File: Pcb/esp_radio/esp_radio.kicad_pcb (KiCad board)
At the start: 2 copper layers, 145.4 x 136.5 mm, 160 parts, among them J1 Power 10V, J10 LCD SPI, J2 JTAG_ESP1, J3 Antenna, J4 USB_B_Micro, J5 GPIOB, J6 GPIOA, J7 MERUS I2S, J8 MERUS I2C, J9 LCD I2C, Q1 SS8050G, Q2 SS8050G, Q3 AO3415A, Q4 SS8050G, SW1 Reset, SW2 Boot, SW3 Prev, SW4 Play, SW5 Next, SW6 RotaryEncoder_Switch, U1 AMS1117-5, U10 AMS1117-1.8, U2 AMS1117-3.3, U3 ESP32-WROVER_IE, U4 VS1053, U5 RDA5807FP, U6 CH340C, U7 MCP23017_SO, U8 74HC157, U9 74HC157, Y1 12.288Mhz, Y2 32.768kHz

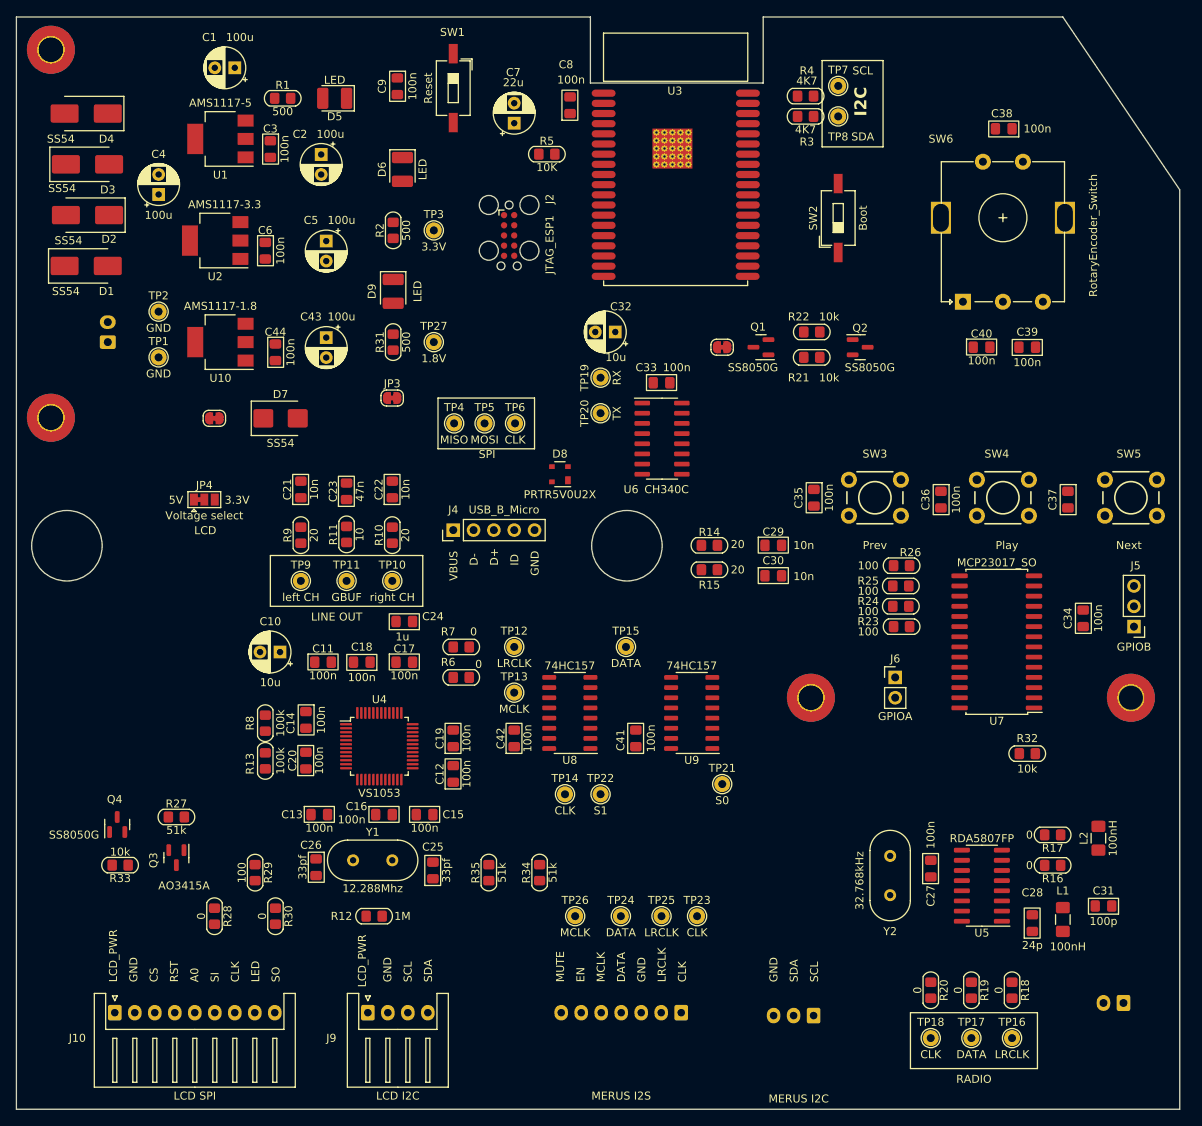
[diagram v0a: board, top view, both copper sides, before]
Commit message: Partially route board
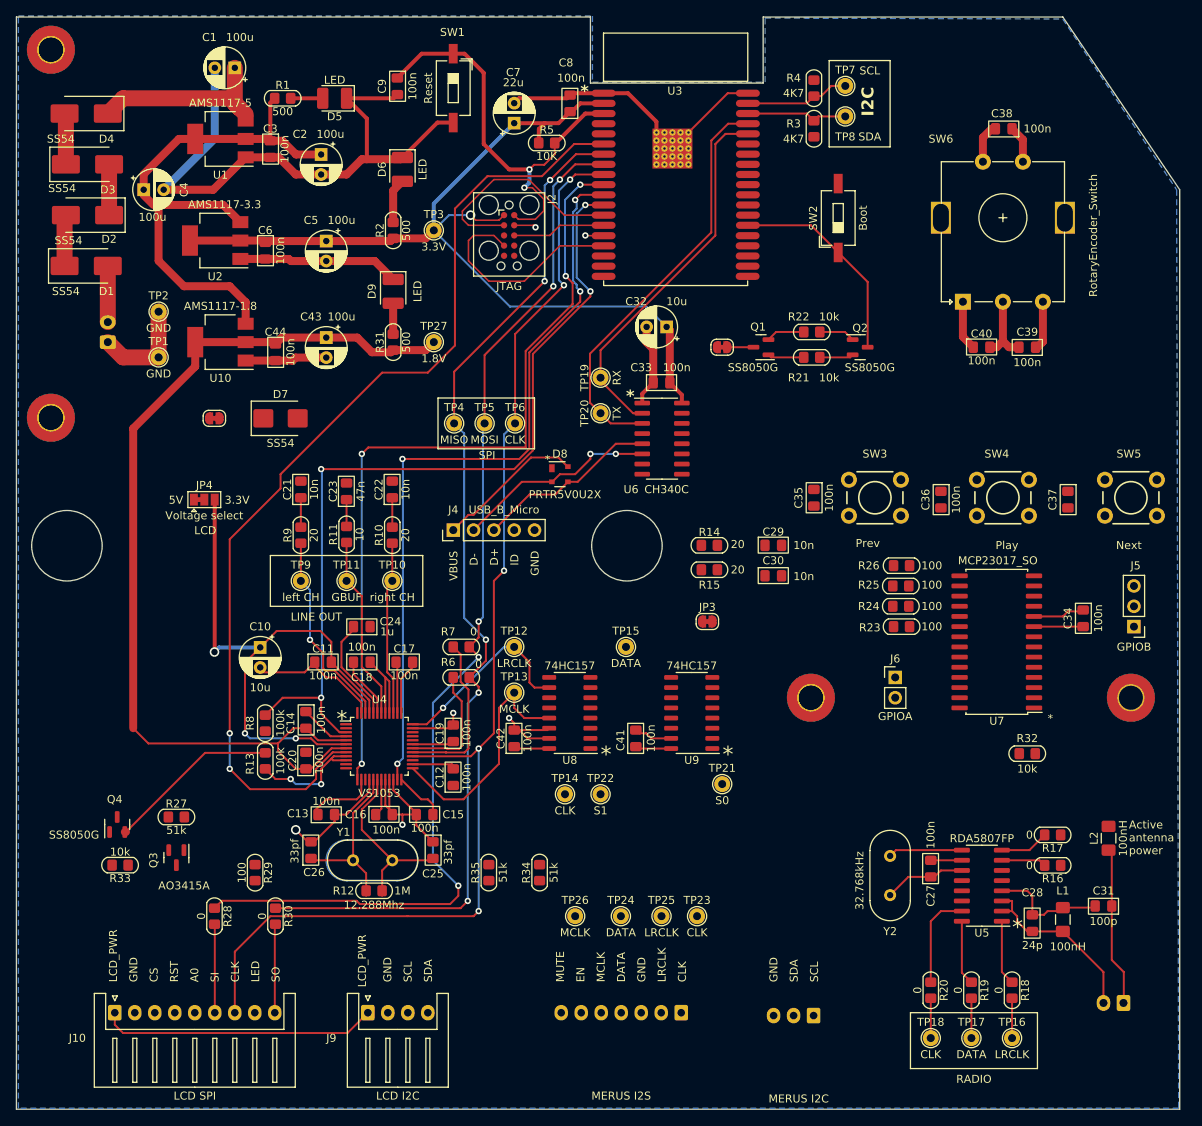
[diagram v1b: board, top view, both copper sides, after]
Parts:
- J2: value JTAG_ESP1 -> JTAG
- moved JP3 48.3 mm to (176.5, 94.6)
- moved C32 6.45 mm to (171.4, 57.8)
- moved C24 5.35 mm to (133.3, 95.2)
- moved R12 3.17 mm to (134.9, 128.3)
- moved C25 2.54 mm to (142.2, 123.2), turned to -90 degrees
- moved C10 2.54 mm to (120.7, 97.9), turned to -90 degrees
- moved C26 2.23 mm to (127.0, 123.2), turned to 90 degrees
- moved C4 1.96 mm to (106.1, 40.6), turned to 0 degrees
- moved R3 1.87 mm to (189.9, 33.0), turned to 90 degrees
- moved R4 1.44 mm to (189.9, 27.9), turned to -90 degrees
- moved R5 1.40 mm to (156.5, 34.8)
- moved L2 1.27 mm to (226.7, 121.7)
- moved TP7 0.88 mm to (193.8, 27.7)
- moved TP8 0.88 mm to (193.8, 31.5)
- moved C13 0.87 mm to (128.9, 118.7), turned to 180 degrees
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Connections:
- ? pad 1: (no net) -> GND (x3)
- REF** pad 1: (no net) -> GND (x4)
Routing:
- net GND: track 0.00 -> 340.4 mm, vias 0 -> 6
- net +3.3V: track 0.00 -> 240.9 mm, vias 0 -> 4
- net /Audio Decoder/SPI.CLK: track 0.00 -> 150.0 mm, vias 0 -> 5
- net /Audio Decoder/SPI.MOSI: track 0.00 -> 136.1 mm, vias 0 -> 5
- net +1V8: track 0.00 -> 134.5 mm
- net /Audio Decoder/SPI.MISO: track 0.00 -> 131.1 mm, vias 0 -> 5
- net /Audio Decoder/VS1053.DREQ: track 0.00 -> 125.2 mm, vias 0 -> 2
- net /Audio Decoder/VS1053.RST: track 0.00 -> 107.2 mm, vias 0 -> 4
- net /Audio Decoder/VS1053.XDCS: track 0.00 -> 101.1 mm, vias 0 -> 4
- net /Audio Decoder/VS1053.XCS: track 0.00 -> 95.0 mm, vias 0 -> 4
- net +5V: track 0.00 -> 69.2 mm
- net /ESP_board/JTAG.RESET: track 0.00 -> 53.3 mm, vias 0 -> 2
- net /ESP_board/UART.TX: track 0.00 -> 52.1 mm
- net /ESP_board/UART.RX: track 0.00 -> 47.0 mm
- net /LCD screen/LCD_PWR: track 0.00 -> 34.6 mm
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- added copper zone on B.Cu, net GND
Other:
- board text added: "*"
- board text added: "Active antenna power"

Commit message: Additional routing
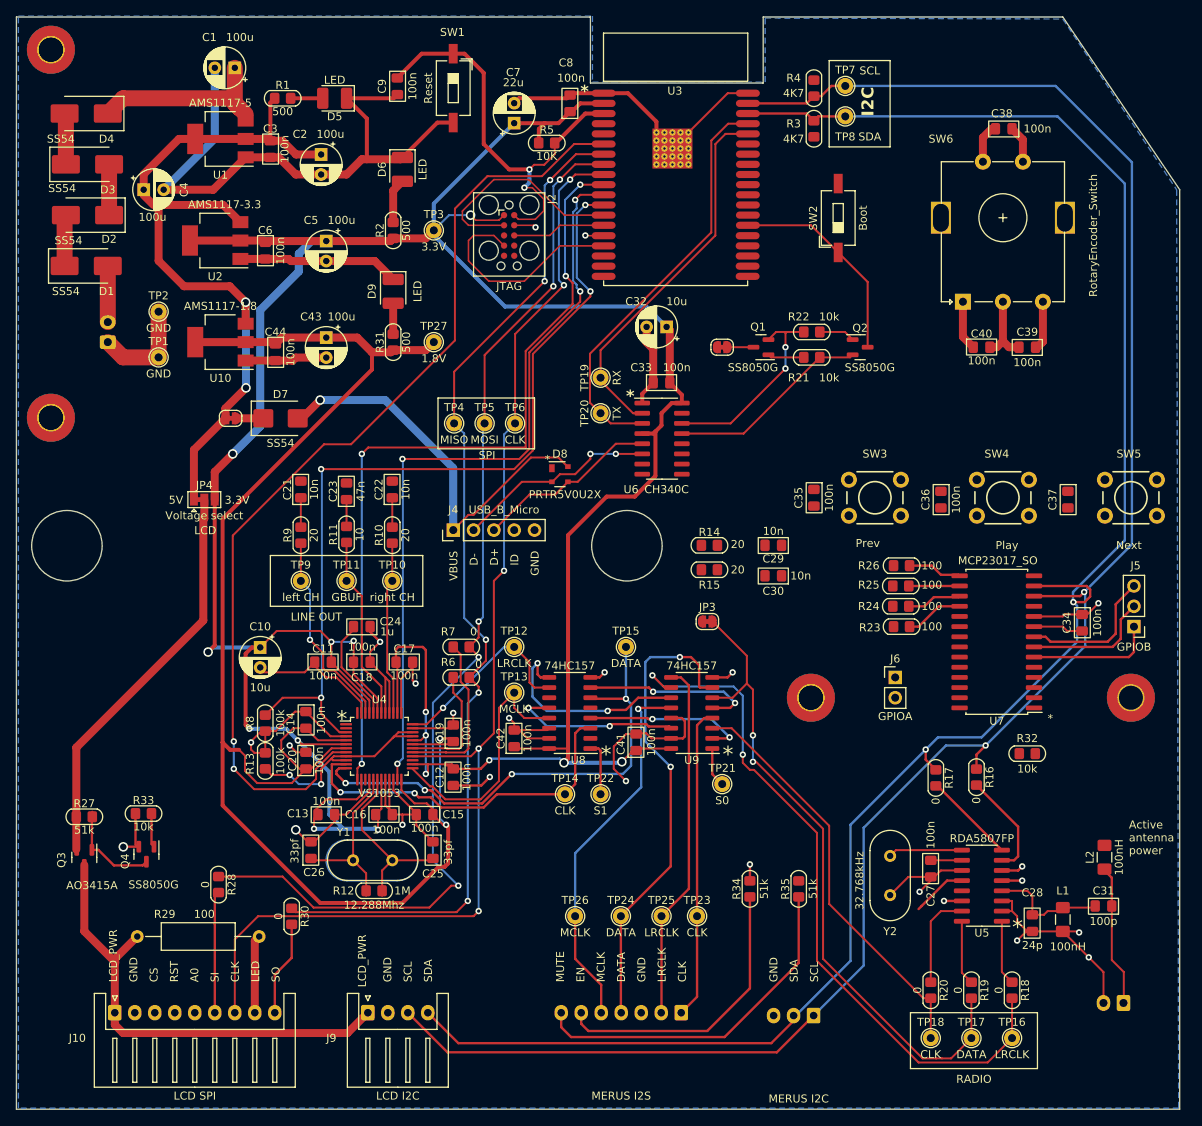
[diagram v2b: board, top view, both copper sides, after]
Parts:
- R29: footprint kicad_common_lib:R_0805 -> Resistor_THT:R_Axial_DIN0309_L9.0mm_D3.2mm_P15.24mm_Horizontal
- moved R35 38.8 mm to (188.0, 128.0)
- moved R34 26.4 mm to (181.9, 128.0)
- moved R29 16.8 mm to (105.3, 134.0), turned to 0 degrees
- moved R17 16.3 mm to (205.1, 114.2), turned to -90 degrees
- moved R16 14.6 mm to (210.2, 114.1), turned to -90 degrees
- moved Q3 11.5 mm to (98.7, 124.1)
- moved R27 11.5 mm to (98.7, 119.0)
- moved R33 7.08 mm to (106.1, 118.6), turned to 0 degrees
- moved Q4 5.21 mm to (106.4, 123.7), turned to -90 degrees
- moved R28 3.99 mm to (115.4, 127.5)
- moved L2 2.43 mm to (226.2, 124.1)
- moved R30 2.03 mm to (124.6, 131.5)
- moved JP1 2.03 mm to (117.0, 69.2)
- moved C34 0.57 mm to (223.4, 94.8)
- moved C41 0.49 mm to (167.6, 109.7)
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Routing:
- net /ESP_board/I2C.SCL: track 13.1 -> 243.6 mm, vias 0 -> 2
- net /ESP_board/I2C.SDA: track 12.8 -> 239.0 mm, vias 0 -> 2
- net +3.3V: track 240.9 -> 420.1 mm, vias 4 -> 15
- net /FM Radio/I2S.LRCLK: track 4.99 -> 88.5 mm, vias 0 -> 2
- net /FM Radio/I2S.DATA: track 4.99 -> 82.9 mm, vias 0 -> 2
- net +1V8: track 134.5 -> 199.8 mm, vias 0 -> 2
- net /Audio Decoder/I2S.DATA: track 0.00 -> 61.6 mm, vias 0 -> 4
- net /I2S Switch/I2SOUT.DATA: track 0.00 -> 59.5 mm, vias 0 -> 2
- net GND: track 340.4 -> 392.1 mm, vias 6 -> 24
- net Net-(JP4-C): track 0.00 -> 50.4 mm
- net /I2S Switch/I2SOUT.MCLK: track 0.00 -> 47.1 mm, vias 0 -> 1
- net /FM Radio/I2S.CLK: track 4.99 -> 52.0 mm
- net /Audio Decoder/I2S.CLK: track 0.00 -> 45.6 mm, vias 0 -> 2
- net /I2S Switch/I2SOUT.LRCLK: track 0.00 -> 45.0 mm
- net /IO Expander/MERUS.MUTE: track 0.00 -> 44.1 mm
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
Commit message: Finish board routing
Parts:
- removed ? (x3): , 
- added C45: 100n, kicad_common_lib:C_0805, F.Cu at (104.2, 67.1)
- added J11: IR, Connector_PinHeader_1.00mm:PinHeader_1x01_P1.00mm_Vertical, F.Cu at (180.2, 55.9)
- added JP5: SolderJumper_2_Bridged, Jumper:SolderJumper-2_P1.3mm_Bridged_RoundedPad1.0x1.5mm, F.Cu at (153.1, 92.5)
- J2: value JTAG -> JTAG_ESP1
- moved C29 58.2 mm to (200.2, 141.2), turned to 90 degrees
- moved R14 56.4 mm to (199.9, 136.5), turned to -90 degrees
- moved C30 53.9 mm to (197.7, 141.2), turned to 90 degrees
- moved R15 52.7 mm to (197.6, 136.5), turned to -90 degrees
- moved R16 4.22 mm to (213.7, 116.3)
- moved R17 3.90 mm to (208.2, 116.6)
- moved R32 1.53 mm to (217.6, 110.0), turned to -90 degrees
- moved R29 0.80 mm to (104.5, 134.2)
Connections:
- J4 pad 4: unconnected-(J4-ID-Pad4) -> Net-(J4-ID)
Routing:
- net +10V: track 7.02 -> 280.0 mm
- net Net-(Q4-B): track 4.27 -> 243.6 mm, vias 0 -> 2
- net +3.3V: track 420.1 -> 623.6 mm, vias 15 -> 23
- net /ESP_board/LCD.CS: track 0.00 -> 171.3 mm, vias 0 -> 2
- net /ESP_board/LCD.A0: track 0.00 -> 161.4 mm, vias 0 -> 2
- net /ESP_board/LCD.RST: track 0.00 -> 159.7 mm, vias 0 -> 2
- net /IO Expander/INT_EXPANDER: track 0.00 -> 116.1 mm, vias 0 -> 2
- net /ESP_board/FM_ST_INT: track 0.00 -> 99.3 mm, vias 0 -> 2
- net /ESP_board/I2S0.CLK: track 0.00 -> 92.1 mm, vias 0 -> 2
- net /ESP_board/I2S0.DATA: track 0.00 -> 85.6 mm, vias 0 -> 2
- net /ESP_board/I2S0.LRCLK: track 0.00 -> 85.3 mm, vias 0 -> 2
- net Net-(U7-GPA5): track 4.68 -> 79.2 mm
- net GND: track 392.1 -> 463.8 mm, vias 24 -> 102
- net /I2S Switch/74HC.S1: track 6.84 -> 68.7 mm, vias 0 -> 1
- net /IO Expander/MERUS.EN: track 36.5 -> 93.8 mm, vias 0 -> 2
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- added copper zone on F.Cu, net GND
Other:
- board text added: "ID/GND"
- board text removed: "ID"

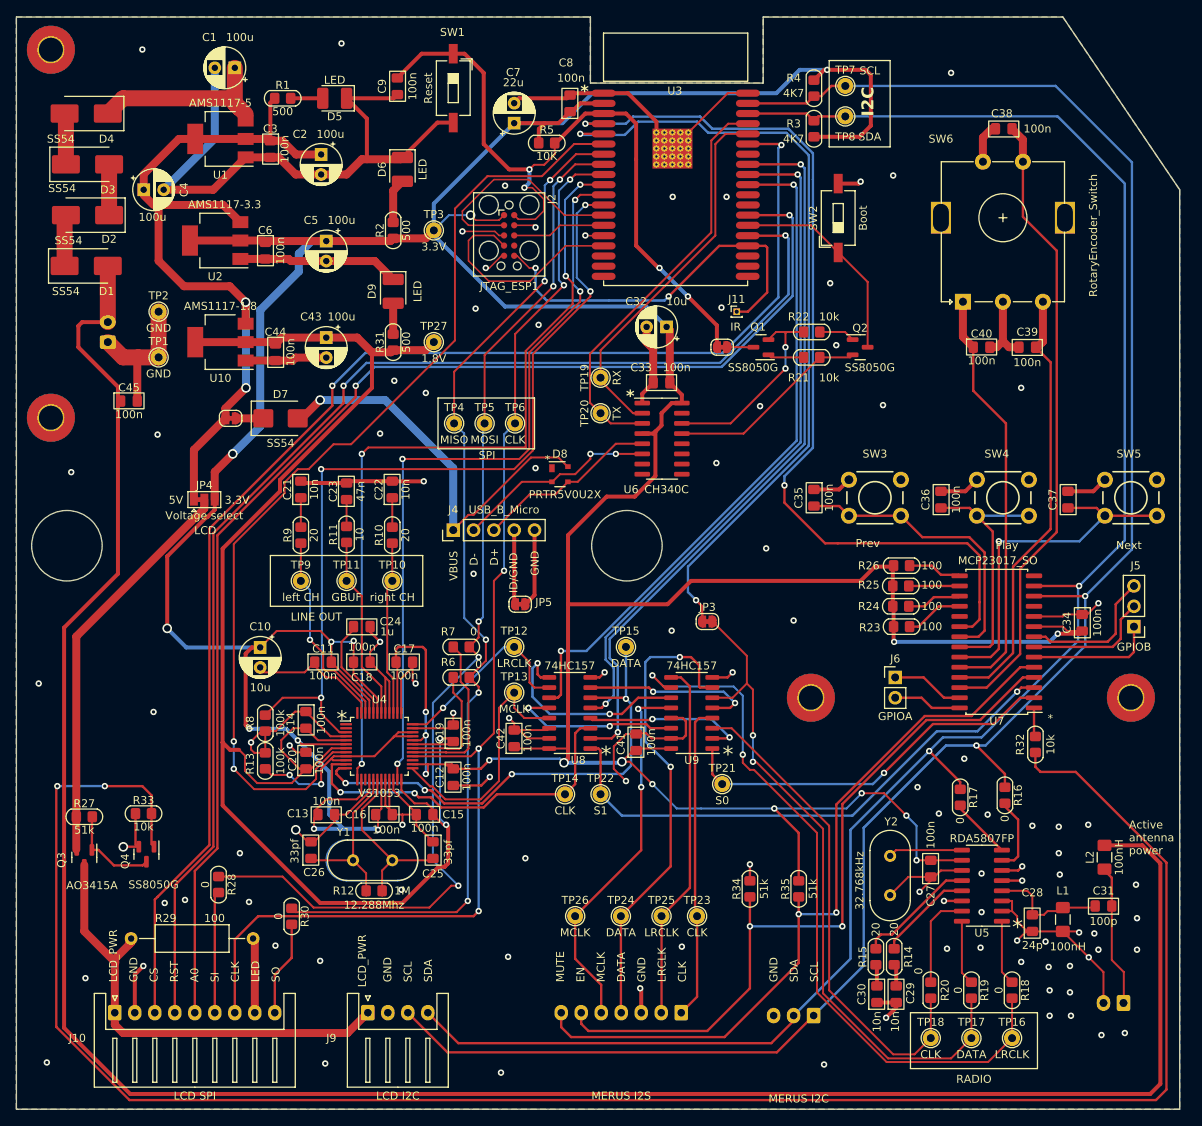
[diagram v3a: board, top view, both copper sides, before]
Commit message: Add chip select emulation for i2c devices
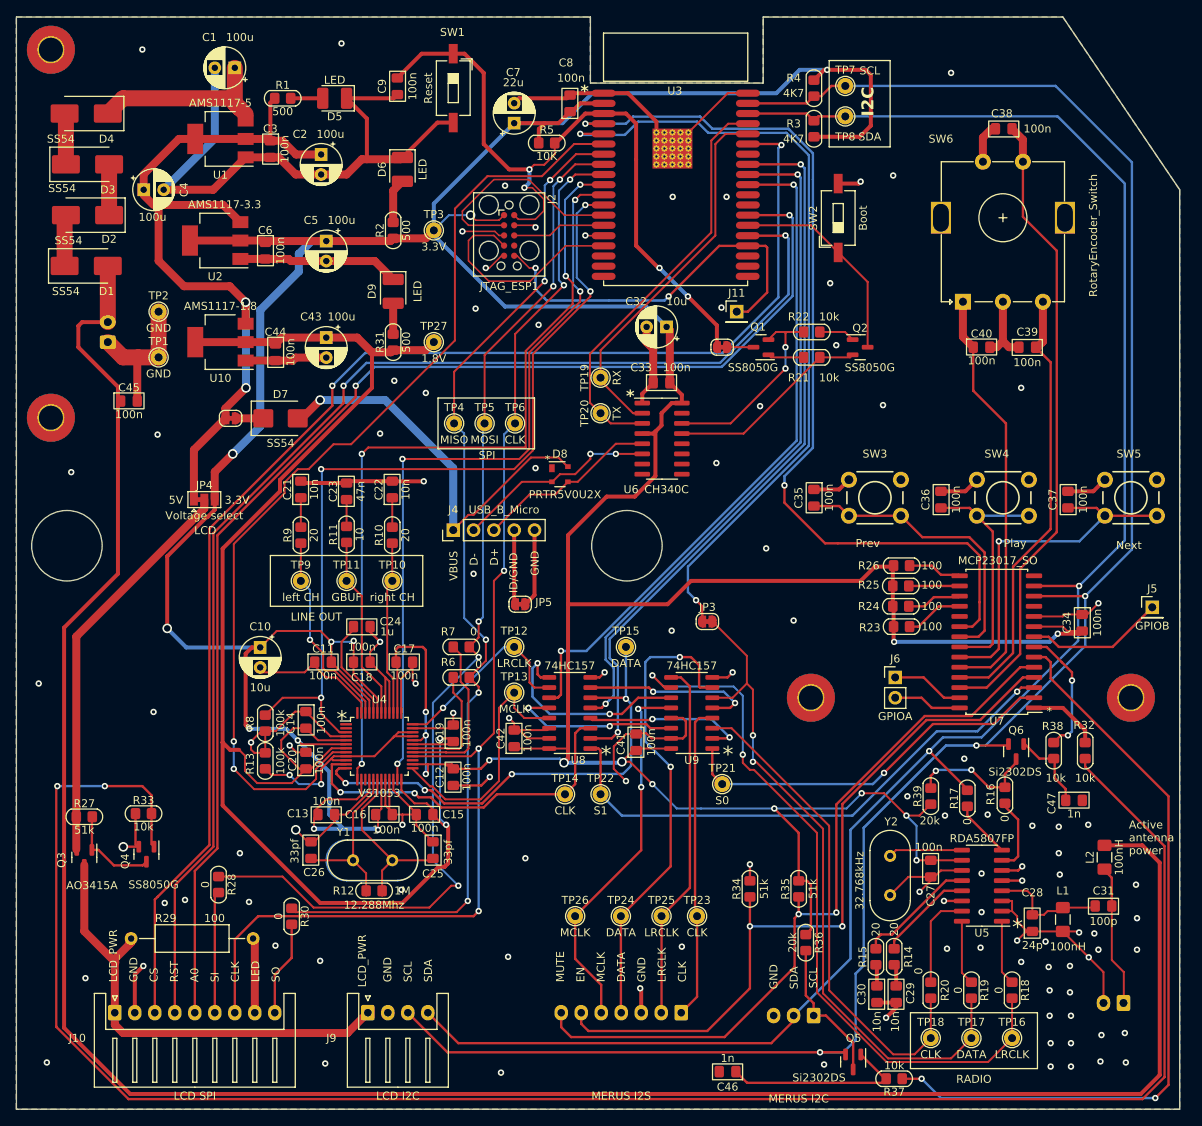
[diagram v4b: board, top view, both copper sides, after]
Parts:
- added C46: 1n, kicad_common_lib:C_0805, F.Cu at (179.1, 150.9)
- added C47: 1n, kicad_common_lib:C_0805, F.Cu at (222.4, 117.0)
- added Q5: Si2302DS, Package_TO_SOT_SMD:SOT-23, F.Cu at (194.8, 149.7)
- added Q6: Si2302DS, Package_TO_SOT_SMD:SOT-23, F.Cu at (215.1, 110.9)
- added R36: 20k, kicad_common_lib:R_0805, F.Cu at (188.8, 134.7)
- added R37: 10k, kicad_common_lib:R_0805, F.Cu at (199.9, 151.8)
- added R38: 10k, kicad_common_lib:R_0805, F.Cu at (219.8, 110.7)
- added R39: 20k, kicad_common_lib:R_0805, F.Cu at (204.5, 116.4)
- J11: footprint Connector_PinHeader_1.00mm:PinHeader_1x01_P1.00mm_Vertical -> Connector_PinHeader_2.54mm:PinHeader_1x01_P2.54mm_Vertical
- J5: footprint Connector_PinHeader_2.54mm:PinHeader_1x03_P2.54mm_Vertical -> Connector_PinHeader_2.54mm:PinHeader_1x01_P2.54mm_Vertical
- moved R32 6.27 mm to (223.8, 110.7)
- moved J5 3.32 mm to (232.2, 92.8), turned to 0 degrees
- moved R17 0.90 mm to (209.0, 116.7)
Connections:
- J8 pad 1: /ESP_board/I2C.SCL -> Net-(J8-Pin_1)
- R16 pad 1: /ESP_board/I2C.SCL -> Net-(Q6-D)
- U7 pad 6: Net-(J5-Pin_1) -> /IO Expander/MerusChipSelect
- U7 pad 7: Net-(J5-Pin_2) -> /FM Radio/FmChipSelect
- U7 pad 8: Net-(J5-Pin_3) -> Net-(J5-Pin_1)
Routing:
- net /IO Expander/MerusChipSelect: track 0.00 -> 96.3 mm, vias 0 -> 2
- net Net-(Q5-G): track 0.00 -> 24.0 mm
- net Net-(J8-Pin_1): track 0.00 -> 18.2 mm
- net Net-(J5-Pin_3): track 17.8 -> 0.00 mm
- net /FM Radio/FmChipSelect: track 0.00 -> 16.3 mm, vias 0 -> 2
- net Net-(Q6-D): track 0.00 -> 16.1 mm, vias 0 -> 2
- net Net-(J5-Pin_2): track 16.0 -> 0.00 mm
- net +3.3V: track 623.6 -> 635.4 mm
- net Net-(Q6-G): track 0.00 -> 10.3 mm
- net Net-(Q4-B): track 243.6 -> 236.3 mm
- net /ESP_board/I2C.SCL: track 246.7 -> 252.3 mm, vias 2 -> 3
- net /LCD screen/LCD_POWER: track 3.64 -> 9.10 mm
- net Net-(J5-Pin_1): track 15.9 -> 17.4 mm
- net +10V: track 280.0 -> 279.2 mm
- net GND: vias 102 -> 108
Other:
- board text added: "(C) Vasily Dybala. v1.0. 2023y"

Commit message: Export gerber file.
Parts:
- Q5, Q6: value Si2302DS -> BSS138
